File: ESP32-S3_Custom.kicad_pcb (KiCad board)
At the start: 2 copper layers, 1 part, among them U1 ESP32-S3-WROOM-1

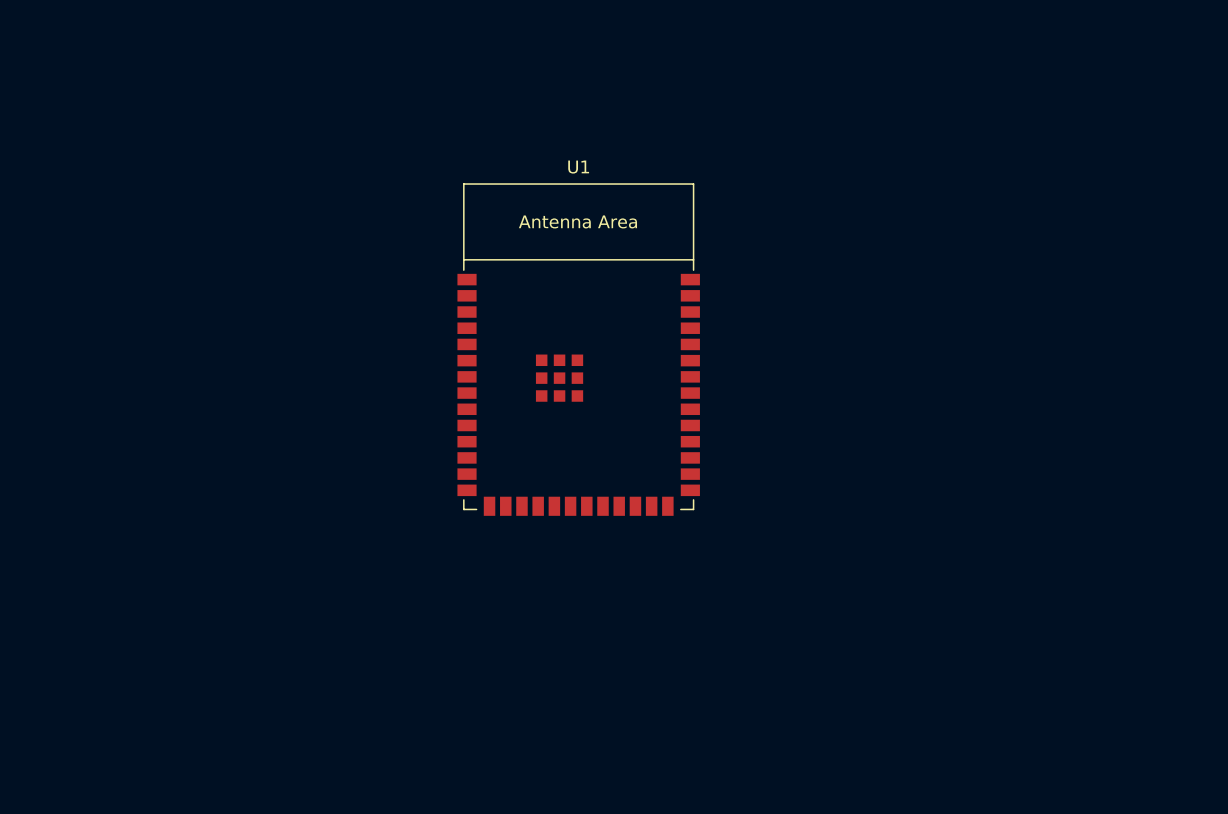
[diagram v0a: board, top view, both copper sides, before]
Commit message: Added components
- USB-C connectors
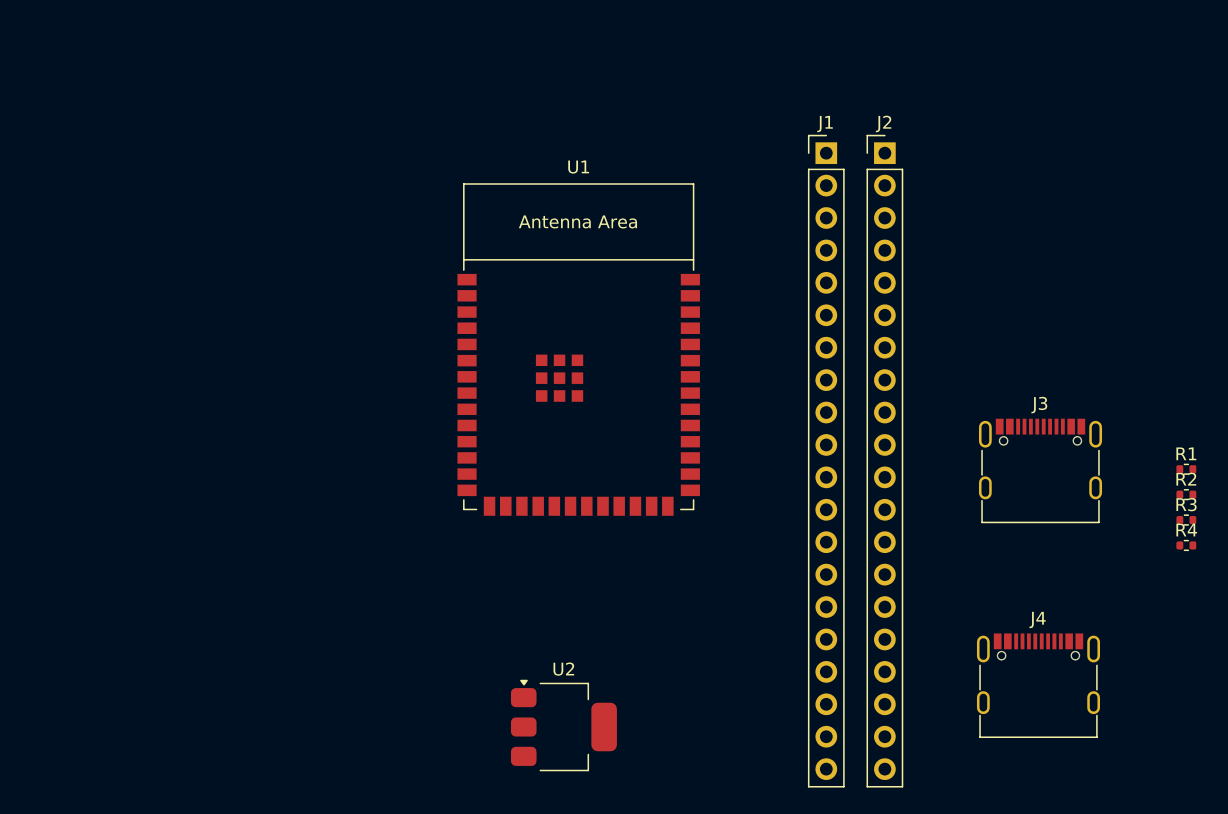
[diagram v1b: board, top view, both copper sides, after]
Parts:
- added J1: Conn_01x20_Pin, Connector_PinHeader_2.54mm:PinHeader_1x20_P2.54mm_Vertical, F.Cu at (162.0, 65.8)
- added J2: Conn_01x20_Pin, Connector_PinHeader_2.54mm:PinHeader_1x20_P2.54mm_Vertical, F.Cu at (166.6, 65.8)
- added J3: USB_C_Receptacle_USB2.0_16P, Connector_USB:USB_C_Receptacle_G-Switch_GT-USB-7010ASV, F.Cu at (178.8, 90.9)
- added J4: USB_C_Receptacle_USB2.0_16P, Connector_USB:USB_C_Receptacle_G-Switch_GT-USB-7010ASV, F.Cu at (178.7, 107.8)
- added R1: 4k7 0402, Resistor_SMD:R_0402_1005Metric, F.Cu at (190.2, 90.5)
- added R2: 4k7 0402, Resistor_SMD:R_0402_1005Metric, F.Cu at (190.2, 92.5)
- added R3: 4k7 0402, Resistor_SMD:R_0402_1005Metric, F.Cu at (190.2, 94.5)
- added R4: 4k7 0402, Resistor_SMD:R_0402_1005Metric, F.Cu at (190.2, 96.5)
- added U2: AMS1117-3.3, Package_TO_SOT_SMD:SOT-223-3_TabPin2, F.Cu at (141.5, 110.7)
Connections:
- U1 pad 2: unconnected-(U1-3V3-Pad2) -> +3.3V

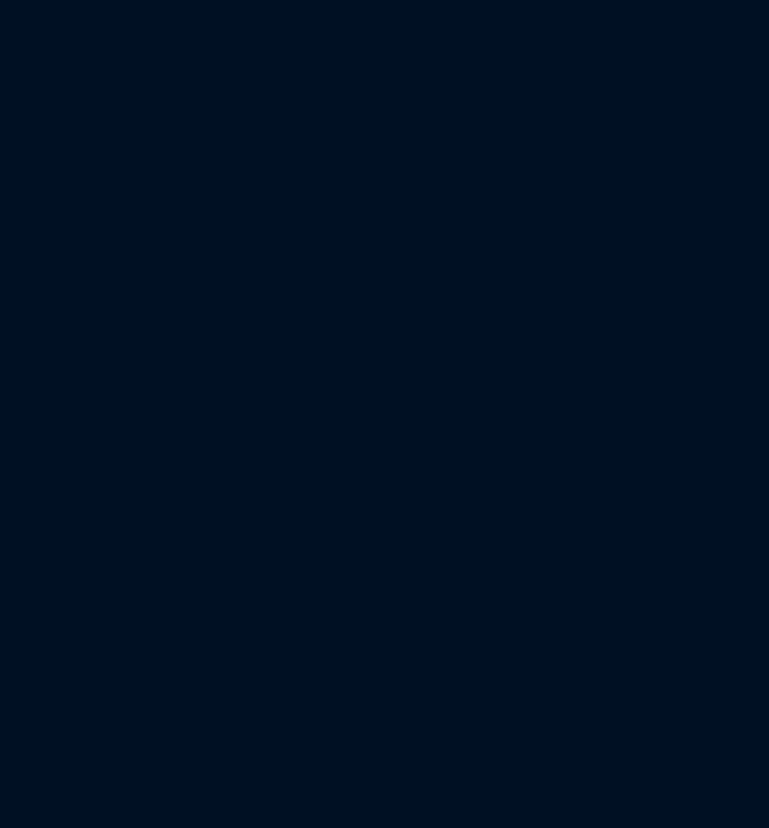
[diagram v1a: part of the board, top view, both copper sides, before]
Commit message: Added TF-01A component
- Added local library support.
  - linked component correctly.

NOTE: proj_foot was not the default for snap.

TODO: Ensure ESP32-S3 WROOM ports correctly
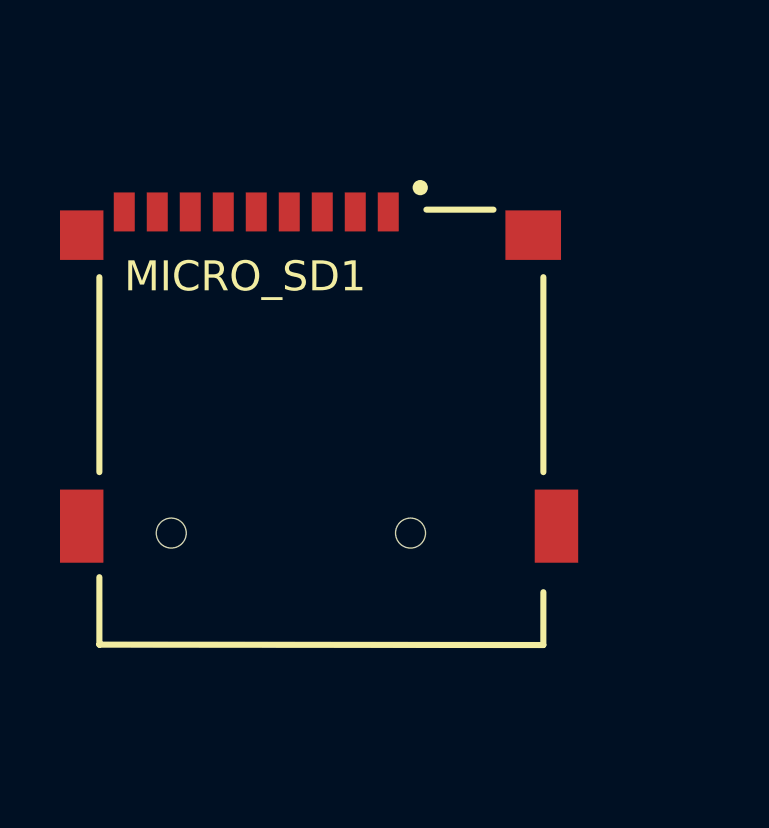
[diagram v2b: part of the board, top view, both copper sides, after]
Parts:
- added MICRO_SD1: TF-01A, proj_foot:TF-01A, F.Cu at (108.0, 93.0)

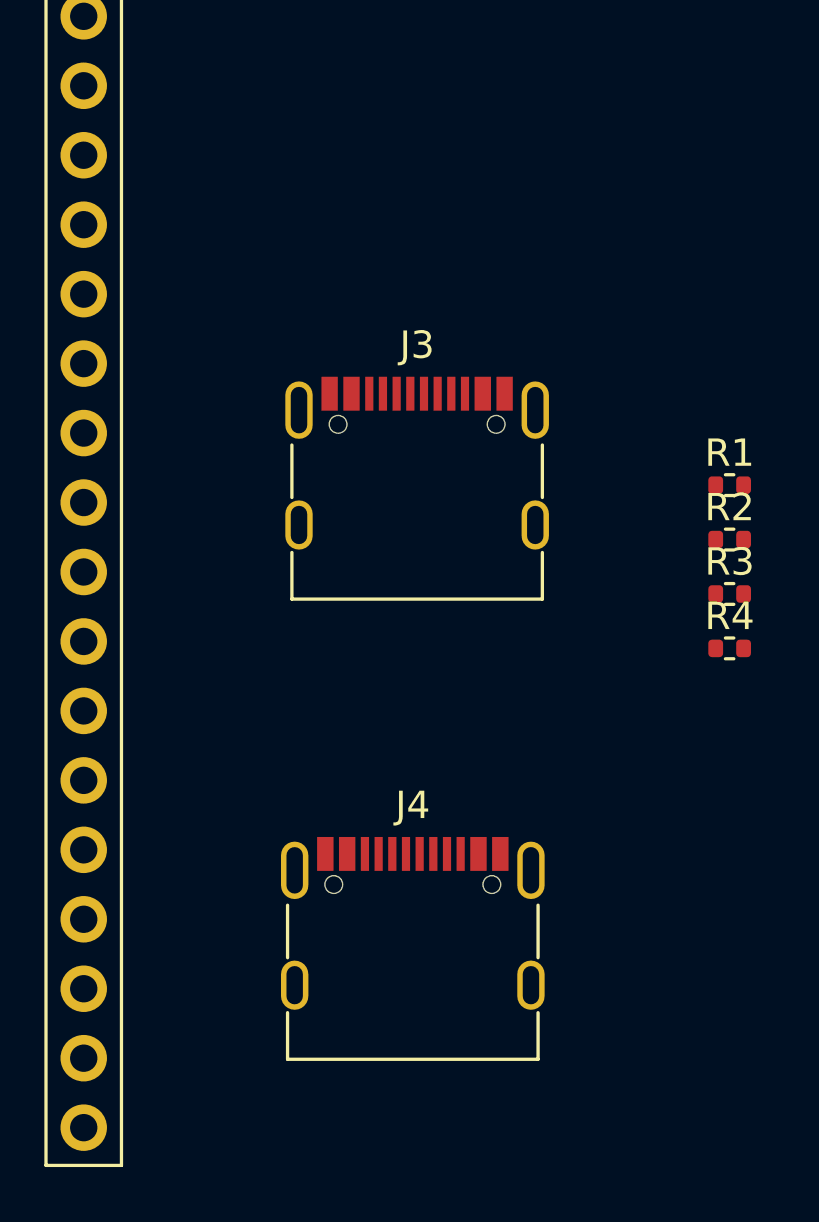
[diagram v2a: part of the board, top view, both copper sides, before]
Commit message: Adjusted 3D model for USB-C connectors
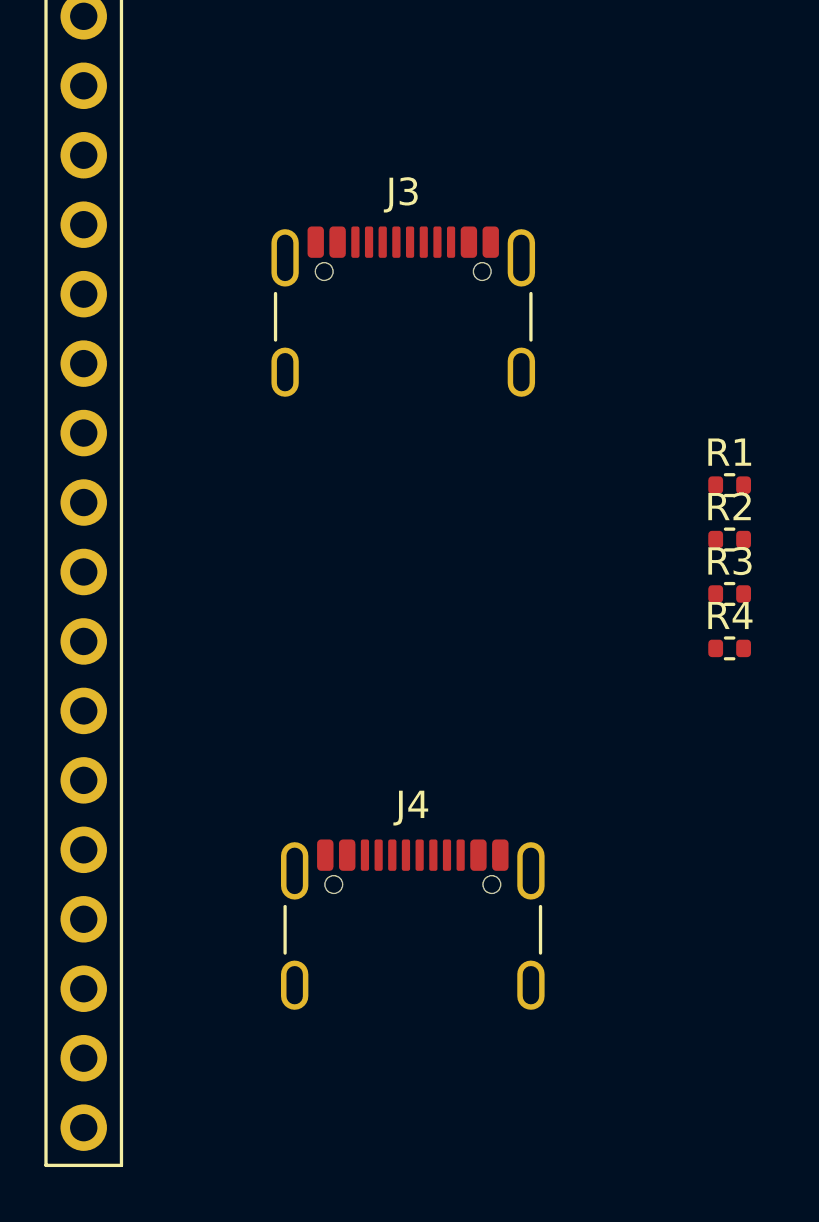
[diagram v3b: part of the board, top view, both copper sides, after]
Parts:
- J3, J4: footprint Connector_USB:USB_C_Receptacle_G-Switch_GT-USB-7010ASV -> Connector_USB:USB_C_Receptacle_GCT_USB4105-xx-A_16P_TopMnt_Horizontal
- moved J3 5.61 mm to (178.3, 85.3)

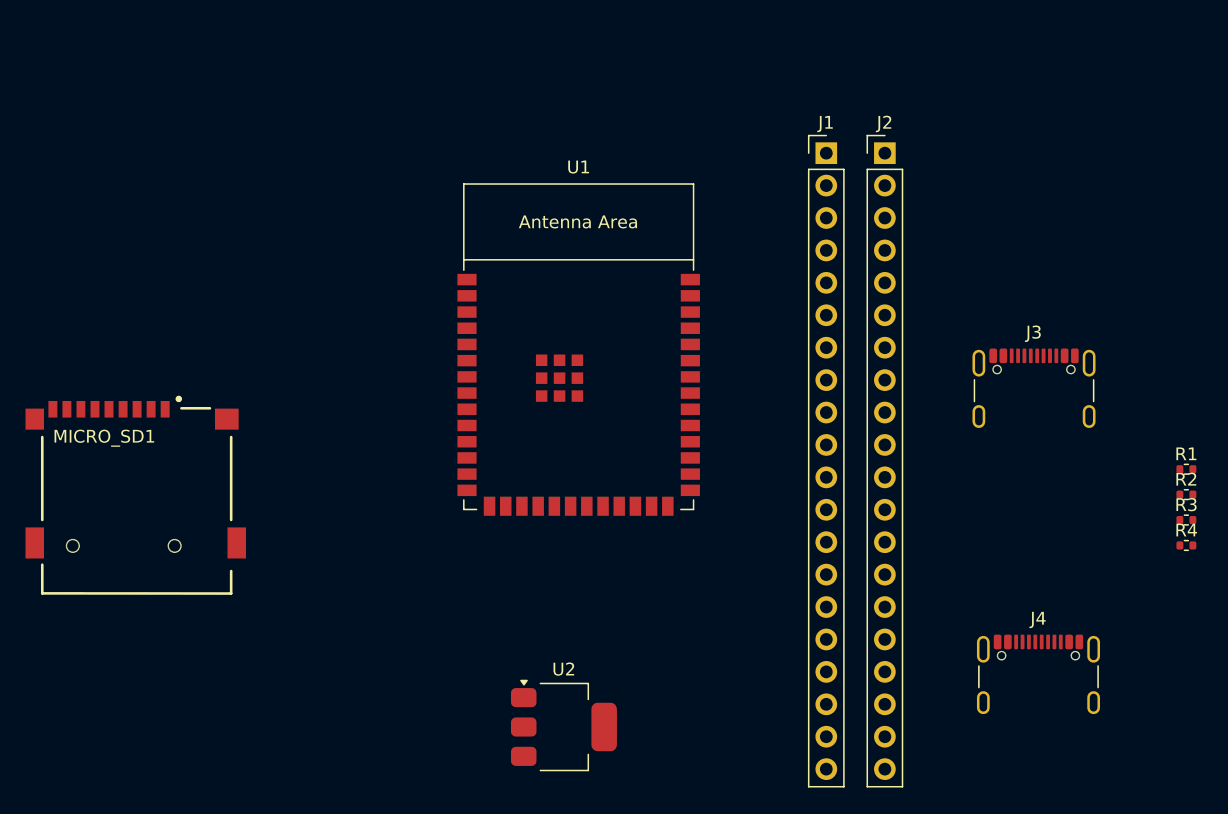
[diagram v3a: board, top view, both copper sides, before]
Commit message: Shuffled some parts around
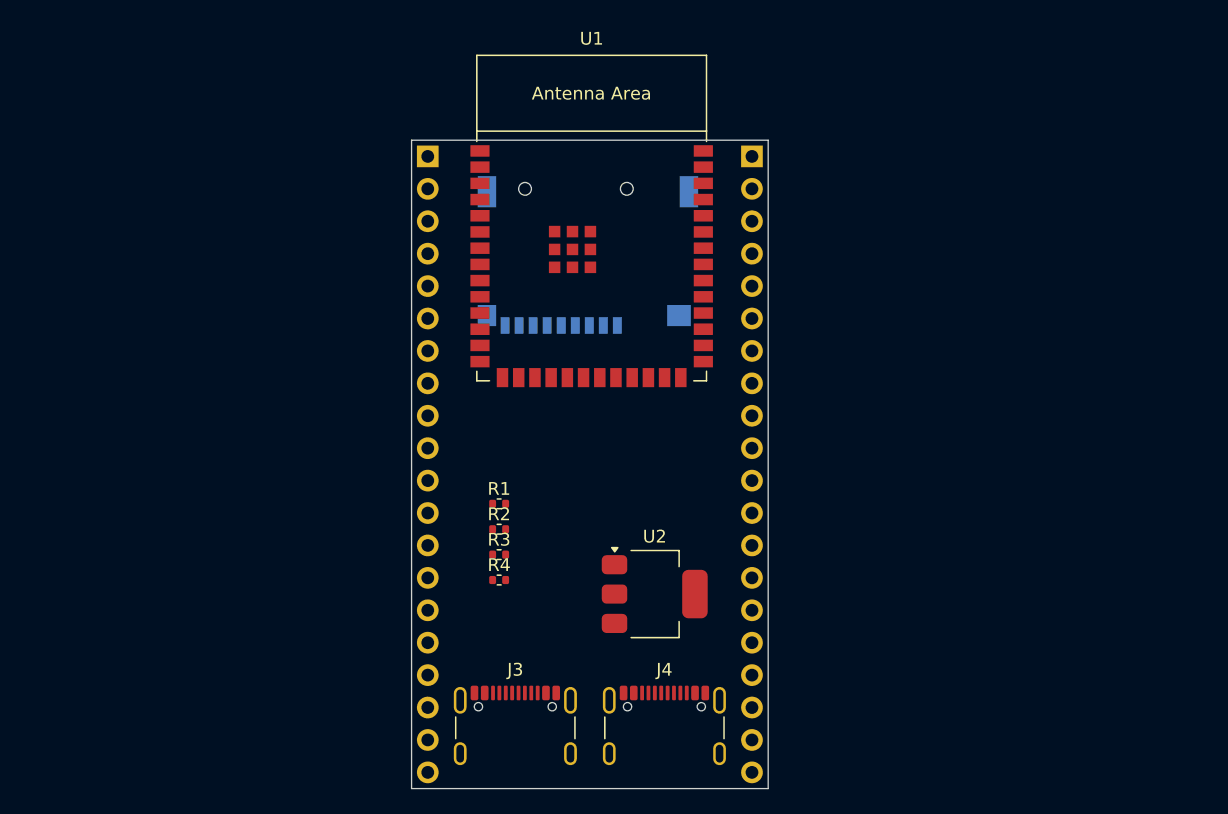
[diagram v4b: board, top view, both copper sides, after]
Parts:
- J1, J2, MICRO_SD1: moved to B.Cu
- moved R1 53.9 mm to (136.4, 93.3)
- moved R2 53.9 mm to (136.4, 95.2)
- moved R3 53.9 mm to (136.4, 97.2)
- moved R4 53.9 mm to (136.4, 99.2)
- moved J3 48.5 mm to (137.7, 111.8)
- moved MICRO_SD1 41.1 mm to (143.4, 72.1)
- moved J2 35.8 mm to (130.8, 66.0), turned to 180 degrees
- moved J4 29.6 mm to (149.3, 111.8)
- moved U2 12.6 mm to (148.6, 100.3)
- moved U1 10.1 mm to (143.7, 73.9)
- moved J1 5.83 mm to (156.2, 66.0), turned to 180 degrees
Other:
- board outline added: 27.9 x 50.8 mm

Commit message: Rotated PCB 90 degrees so its in landscape
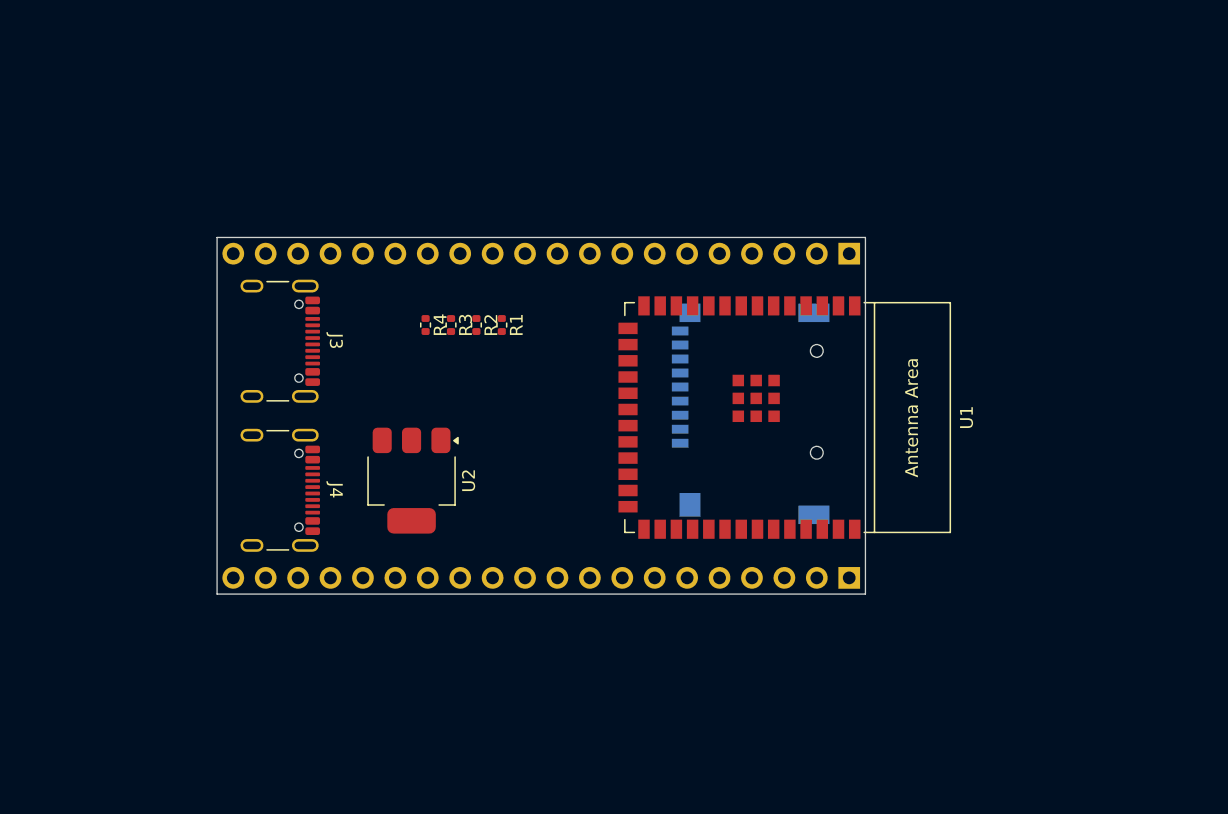
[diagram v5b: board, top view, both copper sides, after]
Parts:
- moved J3 36.9 mm to (118.1, 80.5), turned to -90 degrees
- moved J4 36.9 mm to (118.1, 92.2), turned to -90 degrees
- moved J2 33.9 mm to (163.8, 73.7), turned to 90 degrees
- moved J1 33.9 mm to (163.8, 99.1), turned to 90 degrees
- moved U2 21.0 mm to (129.5, 91.4), turned to -90 degrees
- moved R4 20.8 mm to (130.6, 79.2), turned to -90 degrees
- moved MICRO_SD1 20.2 mm to (157.8, 86.3), turned to -90 degrees
- moved R3 18.4 mm to (132.6, 79.2), turned to -90 degrees
- moved U1 17.7 mm to (156.0, 86.5), turned to -90 degrees
- moved R2 16.1 mm to (134.6, 79.2), turned to -90 degrees
- moved R1 14.0 mm to (136.6, 79.2), turned to -90 degrees
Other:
- board size 27.9 x 50.8 mm -> 50.8 x 27.9 mm
